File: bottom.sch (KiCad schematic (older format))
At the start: 8 parts, among them J6 FFC-0.5MM-6POS, J7 Port_3, J8 Port_4

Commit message: Add PicoBlade connectors
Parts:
- J7, J8: footprint node:port -> Connector_Molex:Molex_PicoBlade_53047-0210_1x02_P1.25mm_Vertical
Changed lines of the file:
@@
 F 0 "J7" H 7330 1867 50  0000 L CNN
 F 1 "Port_3" H 7330 1776 50  0000 L CNN
-F 2 "node:port" H 7250 1875 50  0001 C CNN
+F 2 "Connector_Molex:Molex_PicoBlade_53047-0210_1x02_P1.25mm_Vertical" H 7250 1875 50  0001 C CNN
 F 3 "~" H 7250 1875 50  0001 C CNN
 	1    7250 1875
@@
 F 0 "J8" H 7330 2367 50  0000 L CNN
 F 1 "Port_4" H 7330 2276 50  0000 L CNN
-F 2 "node:port" H 7250 2375 50  0001 C CNN
+F 2 "Connector_Molex:Molex_PicoBlade_53047-0210_1x02_P1.25mm_Vertical" H 7250 2375 50  0001 C CNN
 F 3 "~" H 7250 2375 50  0001 C CNN
 	1    7250 2375

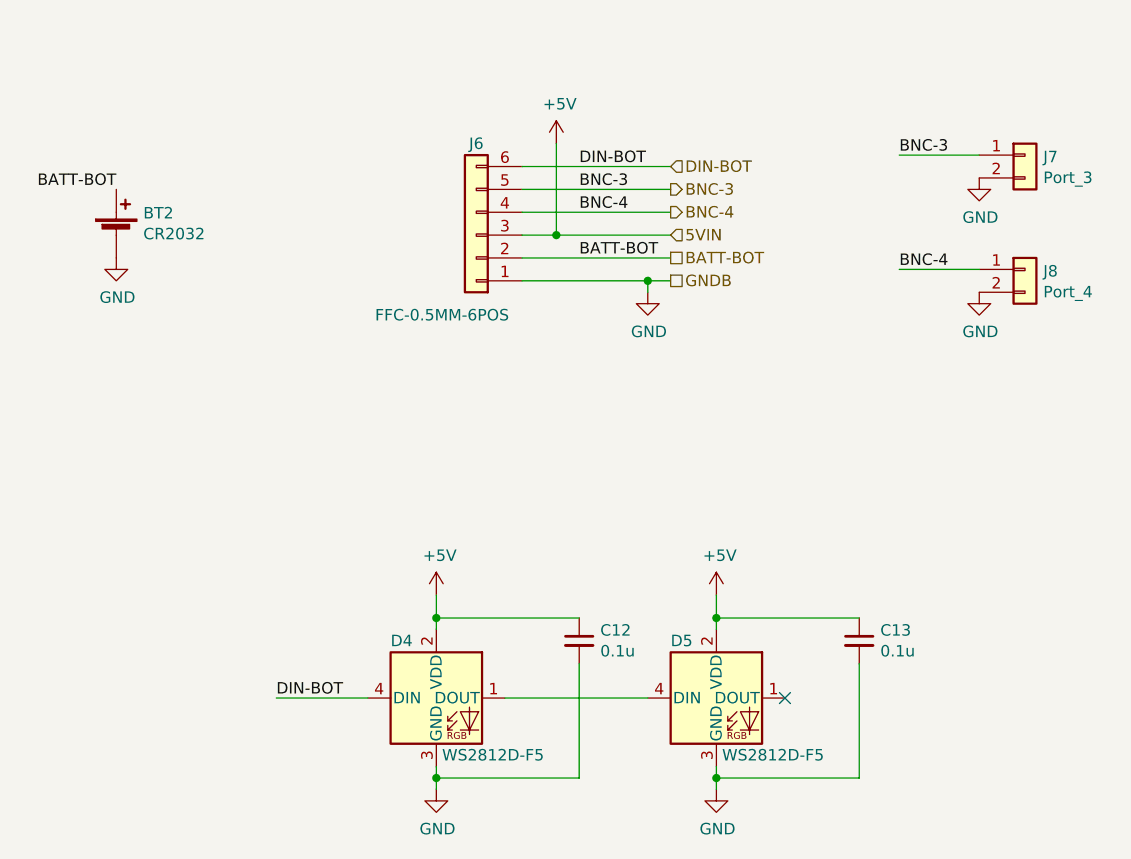
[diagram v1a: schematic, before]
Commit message: Switch to separate power symbols for bottom
Then DRC doesn’t need to know how bottom and top power nets are
connected.
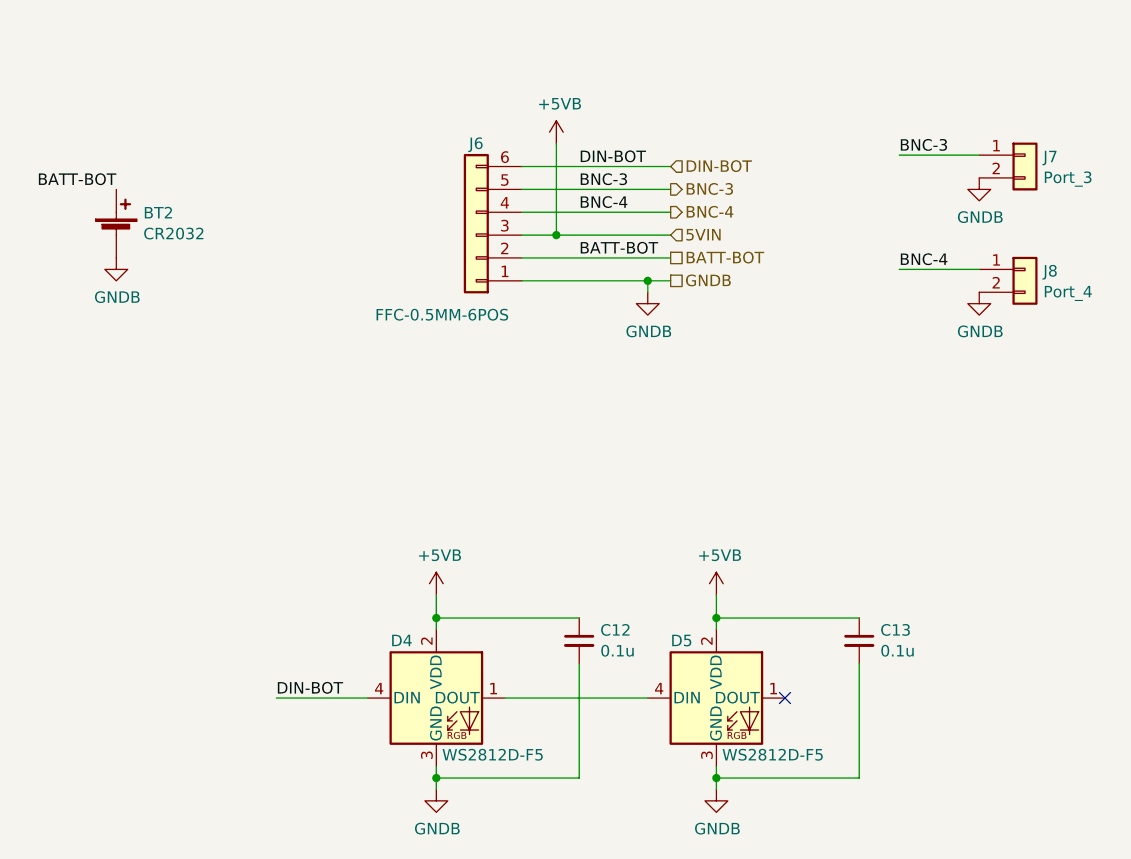
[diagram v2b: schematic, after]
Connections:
- net +5V renamed +5VB
- net GND renamed GNDB
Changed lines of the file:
@@
 Text HLabel 5700 2125 2    50   Output ~ 0
 BNC-4
-Text HLabel 5700 2225 2    50   Input ~ 0
-5VIN
 Text HLabel 5700 2325 2    50   UnSpc ~ 0
 BATT-BOT
 Text HLabel 5700 2425 2    50   UnSpc ~ 0
 GNDB
-$Comp
-L power:GND #PWR0101
-U 1 1 5CA58E18
-P 3275 2325
-F 0 "#PWR0101" H 3275 2075 50  0001 C CNN
-F 1 "GND" H 3280 2152 50  0000 C CNN
-F 2 "" H 3275 2325 50  0001 C CNN
-F 3 "" H 3275 2325 50  0001 C CNN
-	1    3275 2325
-	1    0    0    -1
-$EndComp
 Text Label 3275 2025 2    50   ~ 0
 BATT-BOT
@@
 	1    0    0    -1
 $EndComp
-$Comp
-L power:GND #PWR0102
-U 1 1 5CA792A5
-P 5600 2475
-F 0 "#PWR0102" H 5600 2225 50  0001 C CNN
-F 1 "GND" H 5605 2302 50  0000 C CNN
-F 2 "" H 5600 2475 50  0001 C CNN
-F 3 "" H 5600 2475 50  0001 C CNN
-	1    5600 2475
-	1    0    0    -1
-$EndComp
 Wire Wire Line
 	5600 2425 5700 2425
-$Comp
-L power:+5V #PWR0103
-U 1 1 5CA79E38
-P 5200 1825
-F 0 "#PWR0103" H 5200 1675 50  0001 C CNN
-F 1 "+5V" H 5215 1998 50  0000 C CNN
-F 2 "" H 5200 1825 50  0001 C CNN
-F 3 "" H 5200 1825 50  0001 C CNN
-	1    5200 1825
-	1    0    0    -1
-$EndComp
-Wire Wire Line
-	5200 1825 5200 2225
-Wire Wire Line
-	5200 2225 5700 2225
 Text Label 5300 2125 0    50   ~ 0
 BNC-4
@@
 Wire Wire Line
 	5050 2225 5200 2225
-Connection ~ 5200 2225
 Wire Wire Line
 	5050 2325 5700 2325
@@
 Text Label 6700 2375 0    50   ~ 0
 BNC-4
-$Comp
-L power:GND #PWR0104
-U 1 1 5CA7ED40
-P 7050 2475
-F 0 "#PWR0104" H 7050 2225 50  0001 C CNN
-F 1 "GND" H 7055 2302 50  0000 C CNN
-F 2 "" H 7050 2475 50  0001 C CNN
-F 3 "" H 7050 2475 50  0001 C CNN
-	1    7050 2475
-	1    0    0    -1
-$EndComp
-$Comp
-L power:GND #PWR0105
-U 1 1 5CA7F049
-P 7050 1975
-F 0 "#PWR0105" H 7050 1725 50  0001 C CNN
-F 1 "GND" H 7055 1802 50  0000 C CNN
-F 2 "" H 7050 1975 50  0001 C CNN
-F 3 "" H 7050 1975 50  0001 C CNN
-	1    7050 1975
-	1    0    0    -1
-$EndComp
 Wire Wire Line
 	6700 1875 7050 1875
 Wire Wire Line
 	7050 2375 6700 2375
-$Comp
-L power:+5V #PWR?
-U 1 1 5CA85CAB
-P 4675 3800
-AR Path="/5CA85CAB" Ref="#PWR?"  Part="1"
-AR Path="/5C920754/5CA85CAB" Ref="#PWR?"  Part="1"
-AR Path="/5C920CA4/5CA85CAB" Ref="#PWR037"  Part="1"
-F 0 "#PWR037" H 4675 3650 50  0001 C CNN
-F 1 "+5V" H 4690 3973 50  0000 C CNN
-F 2 "" H 4675 3800 50  0001 C CNN
-F 3 "" H 4675 3800 50  0001 C CNN
-	1    4675 3800
-	1    0    0    -1
-$EndComp
-$Comp
-L power:GND #PWR?
-U 1 1 5CA85CCB
-P 4675 4650
-AR Path="/5CA85CCB" Ref="#PWR?"  Part="1"
-AR Path="/5C920754/5CA85CCB" Ref="#PWR?"  Part="1"
-AR Path="/5C920CA4/5CA85CCB" Ref="#PWR038"  Part="1"
-F 0 "#PWR038" H 4675 4400 50  0001 C CNN
-F 1 "GND" H 4680 4477 50  0000 C CNN
-F 2 "" H 4675 4650 50  0001 C CNN
-F 3 "" H 4675 4650 50  0001 C CNN
-	1    4675 4650
-	1    0    0    -1
-$EndComp
 Wire Wire Line
 	4675 3800 4675 3900
@@
 Wire Wire Line
 	4975 4250 5600 4250
-$Comp
-L power:GND #PWR?
-U 1 1 5CA85CC5
-P 5900 4650
-AR Path="/5CA85CC5" Ref="#PWR?"  Part="1"
-AR Path="/5C920754/5CA85CC5" Ref="#PWR?"  Part="1"
-AR Path="/5C920CA4/5CA85CC5" Ref="#PWR040"  Part="1"
-F 0 "#PWR040" H 5900 4400 50  0001 C CNN
-F 1 "GND" H 5905 4477 50  0000 C CNN
-F 2 "" H 5900 4650 50  0001 C CNN
-F 3 "" H 5900 4650 50  0001 C CNN
-	1    5900 4650
-	1    0    0    -1
-$EndComp
 $Comp
 L Device:C_Small C?
@@
 $EndComp
 $Comp
-L power:+5V #PWR?
-U 1 1 5CA85CB1
-P 5900 3800
-AR Path="/5CA85CB1" Ref="#PWR?"  Part="1"
-AR Path="/5C920754/5CA85CB1" Ref="#PWR?"  Part="1"
-AR Path="/5C920CA4/5CA85CB1" Ref="#PWR039"  Part="1"
-F 0 "#PWR039" H 5900 3650 50  0001 C CNN
-F 1 "+5V" H 5915 3973 50  0000 C CNN
-F 2 "" H 5900 3800 50  0001 C CNN
-F 3 "" H 5900 3800 50  0001 C CNN
-	1    5900 3800
-	1    0    0    -1
-$EndComp
-$Comp
 L node:WS2812D-F5 D?
 U 1 1 5C9C36C4
@@
 $EndComp
 NoConn ~ 6200 4250
+$Comp
+L node:GNDB #PWR0101
+U 1 1 5CA41F18
+P 7050 2475
+F 0 "#PWR0101" H 7050 2225 50  0001 C CNN
+F 1 "GNDB" H 7055 2302 50  0000 C CNN
+F 2 "" H 7050 2475 50  0001 C CNN
+F 3 "" H 7050 2475 50  0001 C CNN
+	1    7050 2475
+	1    0    0    -1
+$EndComp
+$Comp
+L node:GNDB #PWR0102
+U 1 1 5CA4305A
+P 7050 1975
+F 0 "#PWR0102" H 7050 1725 50  0001 C CNN
+F 1 "GNDB" H 7055 1802 50  0000 C CNN
+F 2 "" H 7050 1975 50  0001 C CNN
+F 3 "" H 7050 1975 50  0001 C CNN
+	1    7050 1975
+	1    0    0    -1
+$EndComp
+$Comp
+L node:GNDB #PWR0103
+U 1 1 5CA43459
+P 5600 2475
+F 0 "#PWR0103" H 5600 2225 50  0001 C CNN
+F 1 "GNDB" H 5605 2302 50  0000 C CNN
+F 2 "" H 5600 2475 50  0001 C CNN
+F 3 "" H 5600 2475 50  0001 C CNN
+	1    5600 2475
+	1    0    0    -1
+$EndComp
+$Comp
+L node:GNDB #PWR0104
+U 1 1 5CA437BD
+P 3275 2325
+F 0 "#PWR0104" H 3275 2075 50  0001 C CNN
+F 1 "GNDB" H 3280 2152 50  0000 C CNN
+F 2 "" H 3275 2325 50  0001 C CNN
+F 3 "" H 3275 2325 50  0001 C CNN
+	1    3275 2325
+	1    0    0    -1
+$EndComp
+$Comp
+L node:GNDB #PWR0105
+U 1 1 5CA43F56
+P 4675 4650
+F 0 "#PWR0105" H 4675 4400 50  0001 C CNN
+F 1 "GNDB" H 4680 4477 50  0000 C CNN
+F 2 "" H 4675 4650 50  0001 C CNN
+F 3 "" H 4675 4650 50  0001 C CNN
+	1    4675 4650
+	1    0    0    -1
+$EndComp
+$Comp
+L node:GNDB #PWR0107
+U 1 1 5CA44687
+P 5900 4650
+F 0 "#PWR0107" H 5900 4400 50  0001 C CNN
+F 1 "GNDB" H 5905 4477 50  0000 C CNN
+F 2 "" H 5900 4650 50  0001 C CNN
+F 3 "" H 5900 4650 50  0001 C CNN
+	1    5900 4650
+	1    0    0    -1
+$EndComp
+Wire Wire Line
+	5200 1825 5200 2225
+Text HLabel 5700 2225 2    50   Input ~ 0
+5VIN
+Connection ~ 5200 2225
+Wire Wire Line
+	5200 2225 5700 2225
+$Comp
+L node:+5VB #PWR0108
+U 1 1 5C99193B
+P 5900 3800
+F 0 "#PWR0108" H 5900 3650 50  0001 C CNN
+F 1 "+5VB" H 5915 3973 50  0000 C CNN
+F 2 "" H 5900 3800 50  0001 C CNN
+F 3 "" H 5900 3800 50  0001 C CNN
+	1    5900 3800
+	1    0    0    -1
+$EndComp
+$Comp
+L node:+5VB #PWR0109
+U 1 1 5CA45E8E
+P 4675 3800
+F 0 "#PWR0109" H 4675 3650 50  0001 C CNN
+F 1 "+5VB" H 4690 3973 50  0000 C CNN
+F 2 "" H 4675 3800 50  0001 C CNN
+F 3 "" H 4675 3800 50  0001 C CNN
+	1    4675 3800
+	1    0    0    -1
+$EndComp
+$Comp
+L node:+5VB #PWR0110
+U 1 1 5CA4532B
+P 5200 1825
+F 0 "#PWR0110" H 5200 1675 50  0001 C CNN
+F 1 "+5VB" H 5215 1998 50  0000 C CNN
+F 2 "" H 5200 1825 50  0001 C CNN
+F 3 "" H 5200 1825 50  0001 C CNN
+	1    5200 1825
+	1    0    0    -1
+$EndComp
 $EndSCHEMATC

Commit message: Rename nets, fix ERC warnings and errors
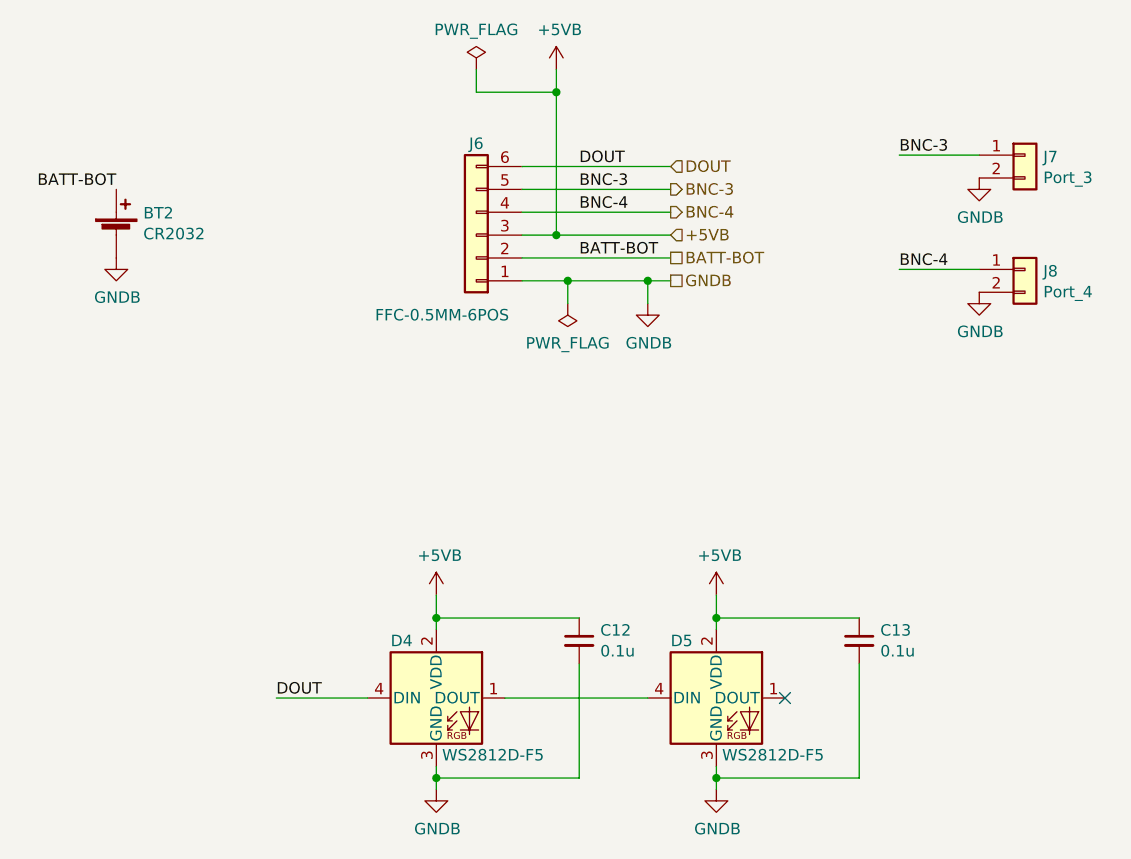
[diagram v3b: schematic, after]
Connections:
- net DIN-BOT renamed DOUT
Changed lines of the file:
@@
 $EndComp
 Text HLabel 5700 1925 2    50   Input ~ 0
-DIN-BOT
+DOUT
 Text HLabel 5700 2025 2    50   Output ~ 0
 BNC-3
@@
 	1    0    0    -1
 $EndComp
-Wire Wire Line
-	5600 2425 5700 2425
 Text Label 5300 2125 0    50   ~ 0
 BNC-4
@@
 BNC-3
 Text Label 5300 1925 0    50   ~ 0
-DIN-BOT
+DOUT
 $Comp
 L Connector_Generic:Conn_01x06 J6
@@
 	5050 2125 5700 2125
 Wire Wire Line
-	5050 2225 5200 2225
-Wire Wire Line
 	5050 2325 5700 2325
-Wire Wire Line
-	5600 2475 5600 2425
-Wire Wire Line
-	5600 2425 5050 2425
-Connection ~ 5600 2425
 Text Label 6700 1875 0    50   ~ 0
 BNC-3
@@
 	7050 2375 6700 2375
 Wire Wire Line
-	4675 3800 4675 3900
-Connection ~ 4675 3900
-Wire Wire Line
 	4675 3900 4675 3950
 Wire Wire Line
@@
 	4675 4600 4675 4650
 Text Label 3975 4250 0    50   ~ 0
-DIN-BOT
+DOUT
 Wire Wire Line
 	3975 4250 4375 4250
@@
 L node:GNDB #PWR0103
 U 1 1 5CA43459
-P 5600 2475
-F 0 "#PWR0103" H 5600 2225 50  0001 C CNN
-F 1 "GNDB" H 5605 2302 50  0000 C CNN
-F 2 "" H 5600 2475 50  0001 C CNN
-F 3 "" H 5600 2475 50  0001 C CNN
-	1    5600 2475
+P 5600 2525
+F 0 "#PWR0103" H 5600 2275 50  0001 C CNN
+F 1 "GNDB" H 5605 2352 50  0000 C CNN
+F 2 "" H 5600 2525 50  0001 C CNN
+F 3 "" H 5600 2525 50  0001 C CNN
+	1    5600 2525
 	1    0    0    -1
 $EndComp
@@
 	1    0    0    -1
 $EndComp
-Wire Wire Line
-	5200 1825 5200 2225
 Text HLabel 5700 2225 2    50   Input ~ 0
-5VIN
-Connection ~ 5200 2225
-Wire Wire Line
-	5200 2225 5700 2225
++5VB
 $Comp
 L node:+5VB #PWR0108
@@
 $EndComp
 $Comp
+L node:+5VB #PWR0110
+U 1 1 5CA4532B
+P 5200 1500
+F 0 "#PWR0110" H 5200 1350 50  0001 C CNN
+F 1 "+5VB" H 5215 1673 50  0000 C CNN
+F 2 "" H 5200 1500 50  0001 C CNN
+F 3 "" H 5200 1500 50  0001 C CNN
+	1    5200 1500
+	1    0    0    -1
+$EndComp
+$Comp
 L node:+5VB #PWR0109
-U 1 1 5CA45E8E
+U 1 1 5CA03EDF
 P 4675 3800
 F 0 "#PWR0109" H 4675 3650 50  0001 C CNN
@@
 	1    0    0    -1
 $EndComp
-$Comp
-L node:+5VB #PWR0110
-U 1 1 5CA4532B
-P 5200 1825
-F 0 "#PWR0110" H 5200 1675 50  0001 C CNN
-F 1 "+5VB" H 5215 1998 50  0000 C CNN
-F 2 "" H 5200 1825 50  0001 C CNN
-F 3 "" H 5200 1825 50  0001 C CNN
-	1    5200 1825
-	1    0    0    -1
-$EndComp
+Wire Wire Line
+	5200 2225 5700 2225
+Wire Wire Line
+	5050 2225 5200 2225
+Connection ~ 5200 2225
+Wire Wire Line
+	5200 1500 5200 1600
+Wire Wire Line
+	4675 3800 4675 3900
+Connection ~ 4675 3900
+Wire Wire Line
+	5050 2425 5250 2425
+Wire Wire Line
+	5600 2525 5600 2425
+Connection ~ 5600 2425
+Wire Wire Line
+	5600 2425 5700 2425
+$Comp
+L power:PWR_FLAG #FLG0101
+U 1 1 5CA08161
+P 4850 1500
+F 0 "#FLG0101" H 4850 1575 50  0001 C CNN
+F 1 "PWR_FLAG" H 4850 1673 50  0000 C CNN
+F 2 "" H 4850 1500 50  0001 C CNN
+F 3 "~" H 4850 1500 50  0001 C CNN
+	1    4850 1500
+	1    0    0    -1
+$EndComp
+Wire Wire Line
+	4850 1500 4850 1600
+Wire Wire Line
+	4850 1600 5200 1600
+Connection ~ 5200 1600
+Wire Wire Line
+	5200 1600 5200 2225
+$Comp
+L power:PWR_FLAG #FLG0102
+U 1 1 5CA09F39
+P 5250 2525
+F 0 "#FLG0102" H 5250 2600 50  0001 C CNN
+F 1 "PWR_FLAG" H 5250 2698 50  0000 C CNN
+F 2 "" H 5250 2525 50  0001 C CNN
+F 3 "~" H 5250 2525 50  0001 C CNN
+	1    5250 2525
+	-1   0    0    1
+$EndComp
+Wire Wire Line
+	5250 2525 5250 2425
+Connection ~ 5250 2425
+Wire Wire Line
+	5250 2425 5600 2425
 $EndSCHEMATC
